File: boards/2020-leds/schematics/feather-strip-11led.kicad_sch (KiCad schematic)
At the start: 14 parts, among them J1 DATA-IN, J2 DATA-OUT, J3 PWR-TAP

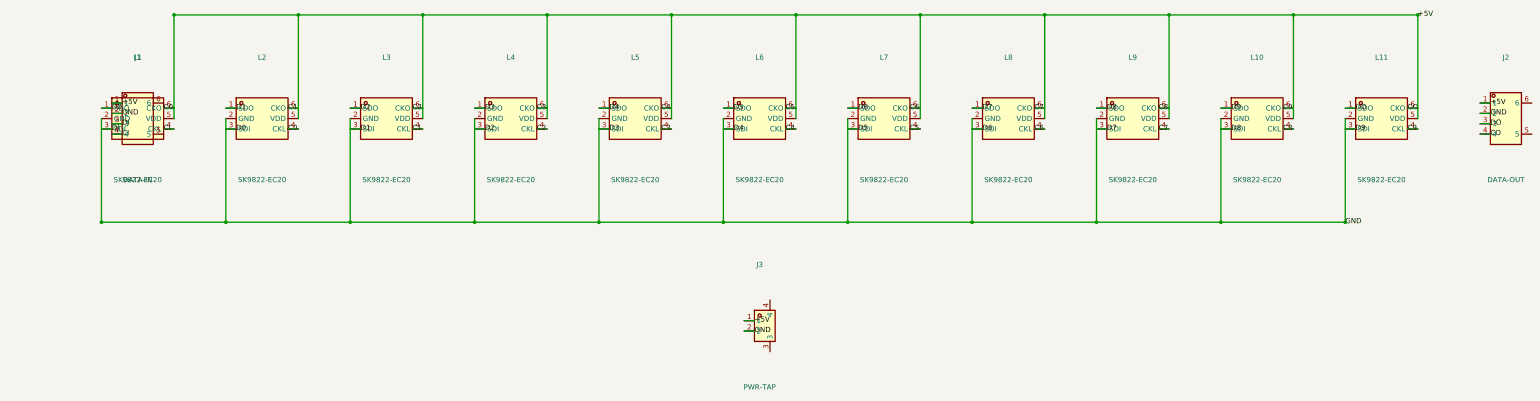
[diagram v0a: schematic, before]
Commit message: tools: feather-strip schematics — LED rot=270 (SDI/GND/SDO top row, CKL/VDD/CKO bottom), GND/VDD straight drops to buses, straight horizontal SDO->SDI & CKO->CLK chain wires with net labels (verified in netlist)
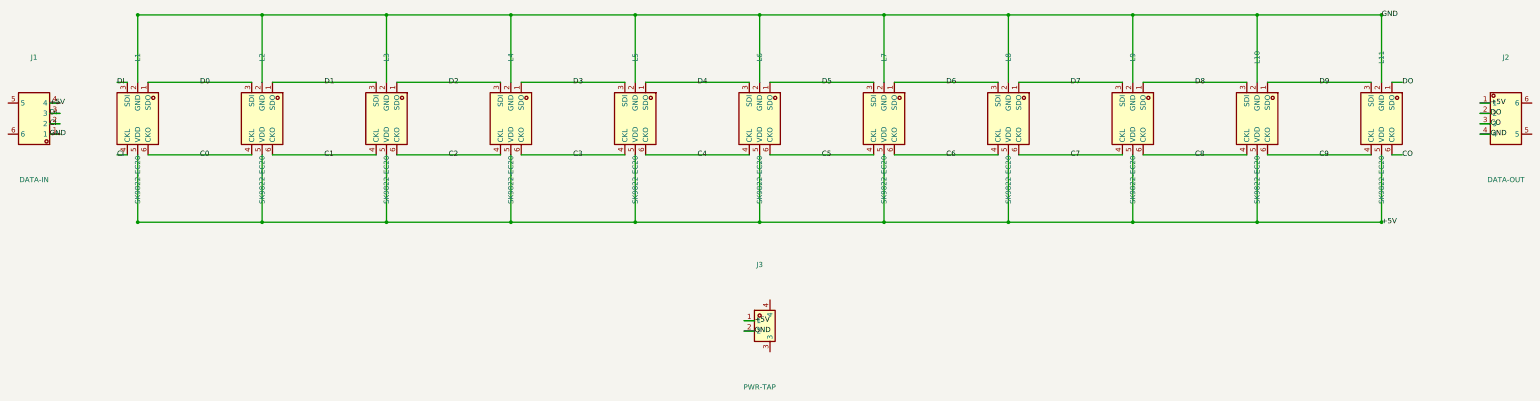
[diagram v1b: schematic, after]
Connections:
- net +5V: now also J1.4; no longer J1.1
- net CI: now also J1.2; no longer J1.4
- net CO: now also J2.3; no longer J2.4
- net DO: now also J2.2; no longer J2.3
- net GND: now also J1.1, J2.4; no longer J1.2, J2.2
